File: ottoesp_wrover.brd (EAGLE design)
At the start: 57.2 x 53.3 mm, 45 parts, among them J1 DC-005, J2 2x3p-2.54, J3 4p-2.54, Q1 S8050, Q2 S8050, Q3 CJ2302, U2 CP2102, U3 CJA1117B-3.3-SOT89, U4 TPD4S012DRYR

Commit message: Updated cap. These have been produced and seem to work. Still testing
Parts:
- C4: value 100nf -> 22uf
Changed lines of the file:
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@@
 <drawing>
 <settings>
-<setting alwaysvectorfont="yes"/>
+<setting alwaysvectorfont="no"/>
 <setting keepoldvectorfont="yes"/>
 <setting verticaltext="up"/>
@@
 <attribute name="VALUE" value="10K" x="51.9609125" y="35.263975" size="1.778" layer="27" rot="R180" display="off"/>
 </element>
-<element name="C4" library="OPL_Capacitor" library_urn="urn:adsk.eagle:library:8004261" package="C0805" package3d_urn="urn:adsk.eagle:package:8004286/1" value="100nf" x="58.550671875" y="30.856346875" smashed="yes" rot="R90">
+<element name="C4" library="OPL_Capacitor" library_urn="urn:adsk.eagle:library:8004261" package="C0805" package3d_urn="urn:adsk.eagle:package:8004286/1" value="22uf" x="58.550671875" y="30.856346875" smashed="yes" rot="R90">
 <attribute name="MPN" value="CC0805KRX7R9BB104" x="58.550671875" y="30.856346875" size="1.778" layer="27" rot="R90" display="off"/>
 <attribute name="NAME" x="56.551346875" y="30.03040625" size="0.3556" layer="25" ratio="11" rot="R90"/>
@@
 <element name="J1" library="OPL_Connector" library_urn="urn:adsk.eagle:library:8004395" package="DCJ3P-14.2X11.0X9.0MM" package3d_urn="urn:adsk.eagle:package:8004506/1" value="DC-005" x="22.877496875" y="44.30505" smashed="yes" rot="R270">
 <attribute name="MPN" value="DC-005" x="22.877496875" y="44.30505" size="1.778" layer="27" rot="R270" display="off"/>
+<attribute name="NAME" x="22.242496875" y="44.30505" size="0.254" layer="33" ratio="10"/>
 <attribute name="NAME" x="16.280165625" y="50.577425" size="0.889" layer="25" ratio="11"/>
-<attribute name="NAME" x="22.242496875" y="44.30505" size="0.254" layer="33" ratio="10"/>
 <attribute name="VALUE" x="22.242496875" y="53.83005" size="0.889" layer="27" ratio="11" rot="R270"/>
 </element>

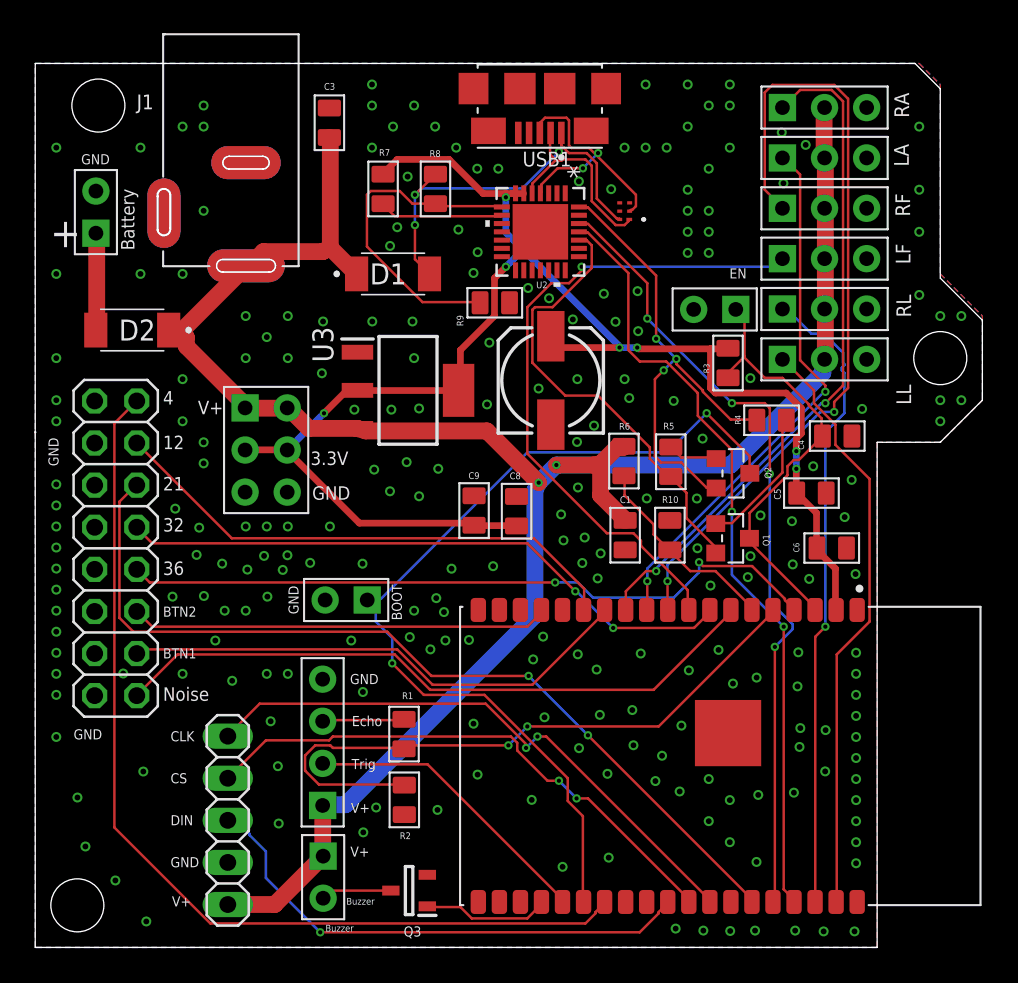
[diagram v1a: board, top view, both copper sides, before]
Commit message: Changed to bew PCB with cutout on corner changed cap to 22uf
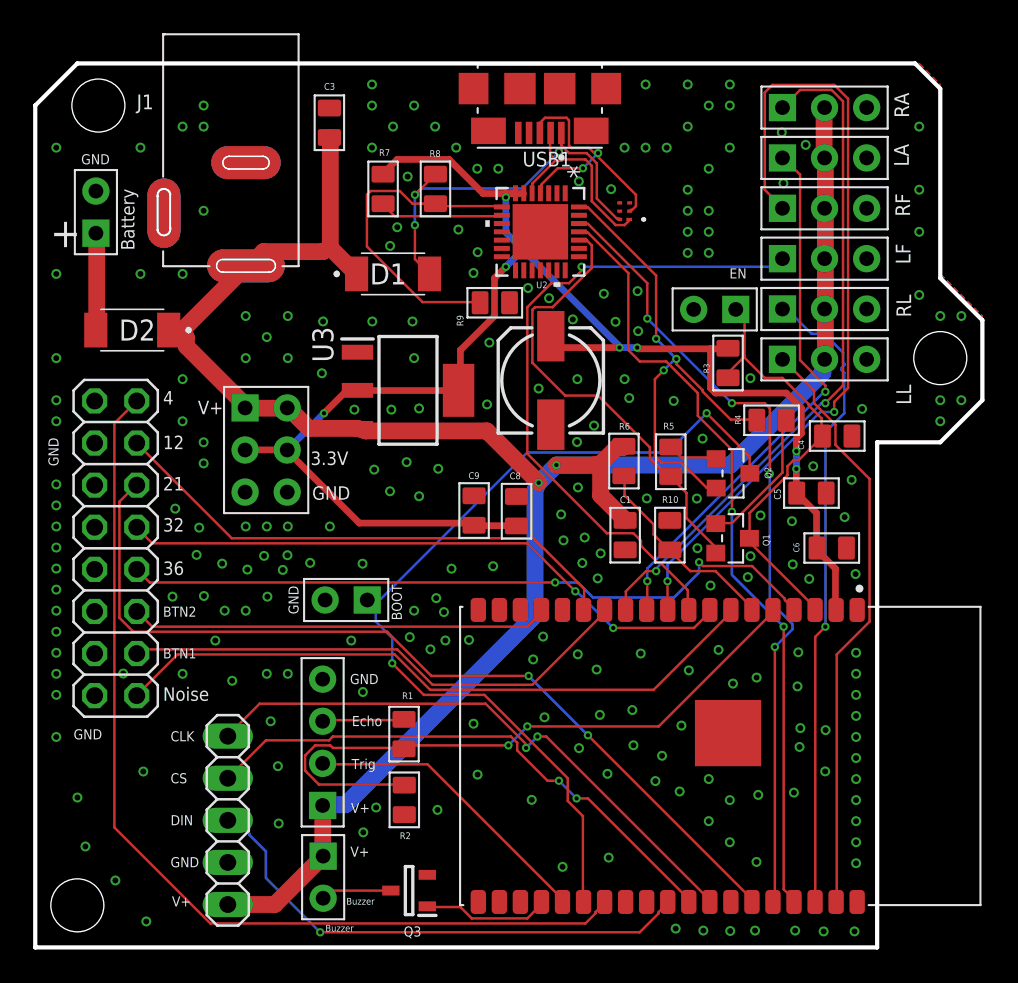
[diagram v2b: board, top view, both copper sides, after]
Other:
- outline, holes or cut-outs redrawn

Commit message: Moved the servo pins and some others closer together to allow the use of pin strips.
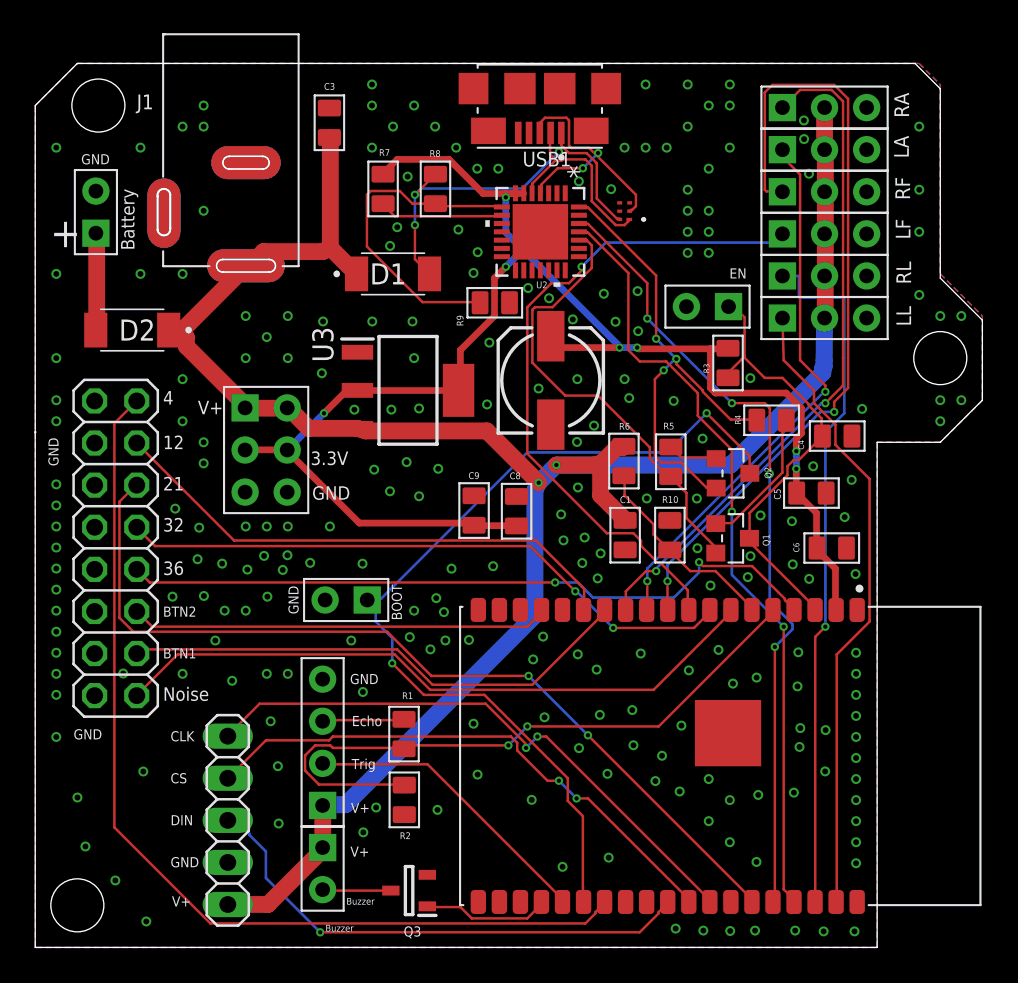
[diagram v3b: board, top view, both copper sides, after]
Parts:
- moved LL 2.49 mm to (57.8, 38.0)
- moved RL 2.00 mm to (57.8, 40.5)
- moved LF 1.50 mm to (57.8, 43.1)
- moved RF 1.00 mm to (57.8, 45.6)
- moved JP3 0.52 mm to (27.5, 4.76)
- moved LA 0.50 mm to (57.8, 48.1)
- moved JP4 0.47 mm to (50.7, 38.7)
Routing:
- net SERVO2: track 38.8 -> 42.2 mm
- net SERVO1: track 35.8 -> 38.2 mm
- net SERVO3: track 40.1 -> 40.7 mm

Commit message: Latest board with 3d packages
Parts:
- A1: device ESP32-WROVER-I:XCVR_ESP32-WROVER-I -> SamacSys_Parts:XCVR_ESP32-WROVER-I
- C1, C3, C5: device Seeed-Capacitor:C0805 -> SamacSys_Parts:C0805
- C2: device OPL_Capacitor:ELECTRO-SMD-C-6MM -> SamacSys_Parts:ELECTRO-SMD-C-6MM
- C4, C6, C8, C9: device OPL_Capacitor:C0805 -> SamacSys_Parts:C0805
- FRAME1: device SparkFun-Aesthetics:MISHAFARMS -> SamacSys_Parts:MISHAFARMS
- J2: device OPL_Connector:H2X3-2.54 -> SamacSys_Parts:H2X3-2.54
- J3: device OPL_Connector:H4-2.54 -> SamacSys_Parts:H4-2.54
- JP2, JP3, JP4, JP5: device OPL_Connector:H2-2.54 -> SamacSys_Parts:H2-2.54
- JP6: device pinhead:1X05 -> SamacSys_Parts:1X05
- LA, LF, LL, RF, RL: value Servo -> 3p-2.54; device OPL_Connector:H3-2.54 -> SamacSys_Parts:H3-2.54
- Q1, Q2: value S8050 -> S8050-G; device OPL_Discrete_Semiconductor:SOT-23 -> SamacSys_Parts:SOT-23
- R1, R10, R2, R3, R4, R5, R6, R7, R8, R9: device OPL_Resistor:R0805 -> SamacSys_Parts:R0805
- RA: value Servos -> 3p-2.54; device OPL_Connector:H3-2.54 -> SamacSys_Parts:H3-2.54
- U2: device cp2102:QFN28N5X5-0P5P -> SamacSys_Parts:QFN28N5X5-0P5P
- USB1: device XLibrary:HRS_ZX62-B-5PA(33) -> SamacSys_Parts:HRS_ZX62-B-5PA(33)
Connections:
- net GND: now also J1.-1B, J1.-1T, J1.-2B; no longer J1.-1
- net V+: now also J1.+B, J1.+T; no longer J1.+
